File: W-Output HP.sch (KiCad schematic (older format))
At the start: 92 parts, among them J1 Conn_01x10, J2 Conn_01x08, J3 Conn_01x03, J4 NC3MBH-1, J5 NC3MBH-1, K1 G6K-2, K2 G6K-2, Q1 MMBT3906, Q2 MMBT3904, Q3 MMBT3904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

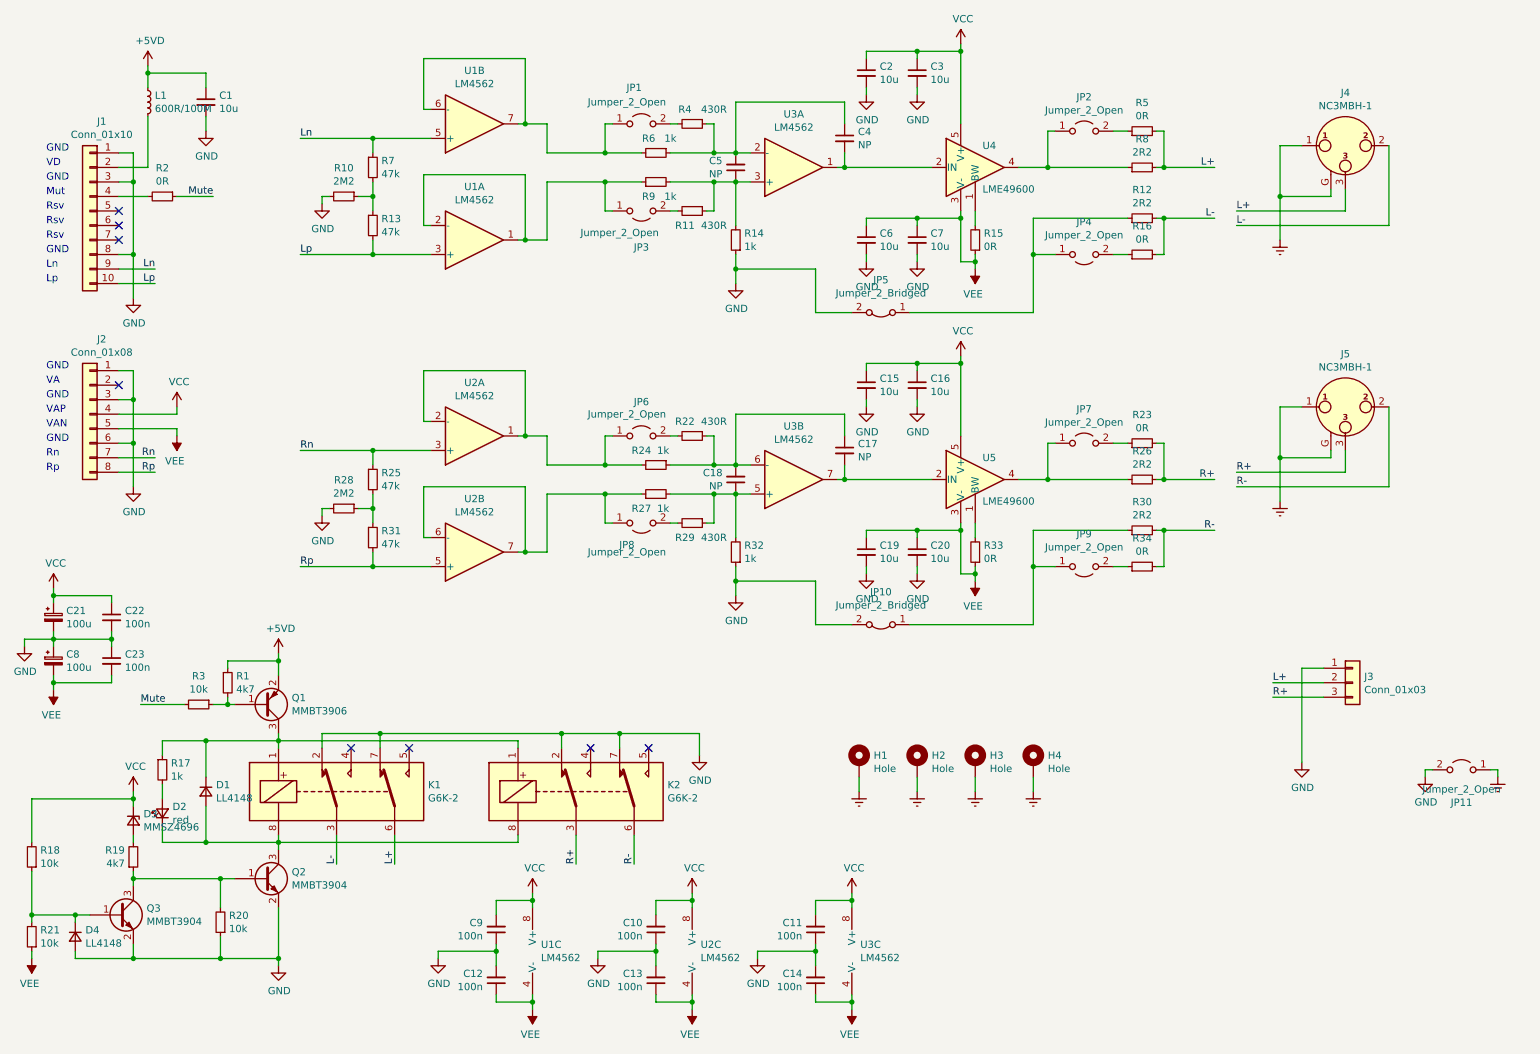
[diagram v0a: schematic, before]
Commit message: Add missing feedback resistor
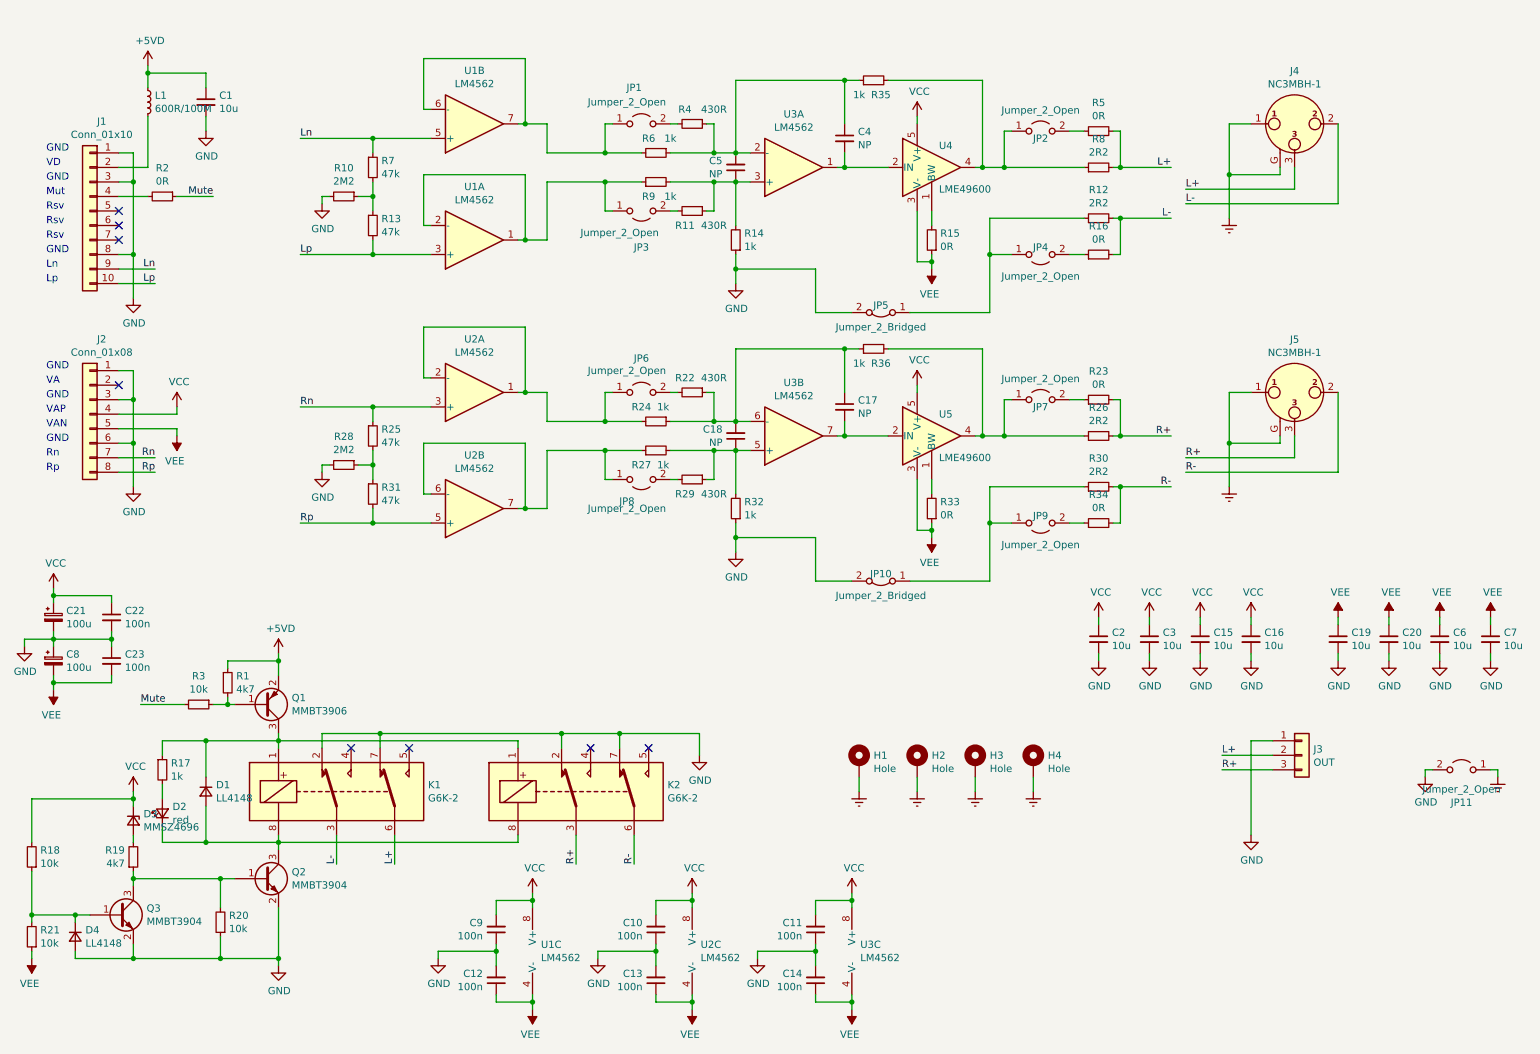
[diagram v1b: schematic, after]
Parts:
- added R35, R36: 1k, Resistor_SMD:R_0603_1608Metric, symbol Device:R_Small
- J3: value Conn_01x03 -> OUT
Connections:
- net at C4.1, C5.2, R4.1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: now also R35.1
- net at JP2.1 (A), R8.1, U4.4: now also R35.2
- net at C17.1, C18.2, R22.1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: now also R36.1
- net at JP7.1 (A), R26.1, U5.4: now also R36.2
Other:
- moved on the sheet: C15, C16, C17, C18, C19, C2, C20, C3, C6, C7, J3, J4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
